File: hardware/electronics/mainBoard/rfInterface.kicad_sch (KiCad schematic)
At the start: 21 parts, among them J15 CONMHF1-SMD-T, J16 CONMHF1-SMD-T, J17 CONMHF1-SMD-T, J18 CONMHF1-SMD-T, U17 PMA2-162LNA+, U18 QCN-19D+

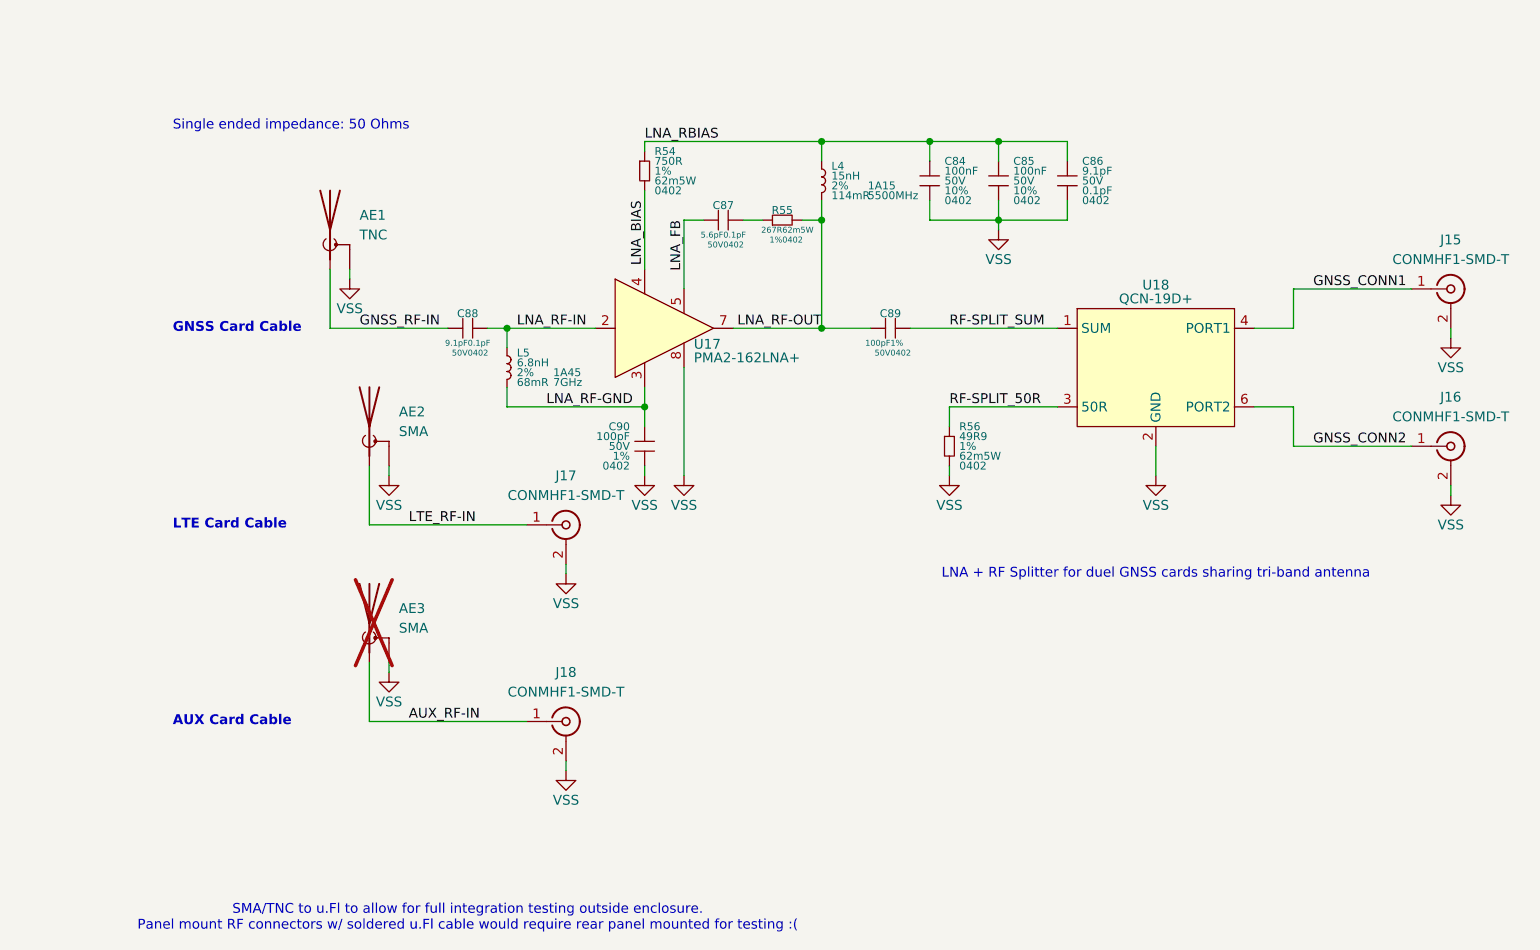
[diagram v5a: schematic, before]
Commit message: renumber references
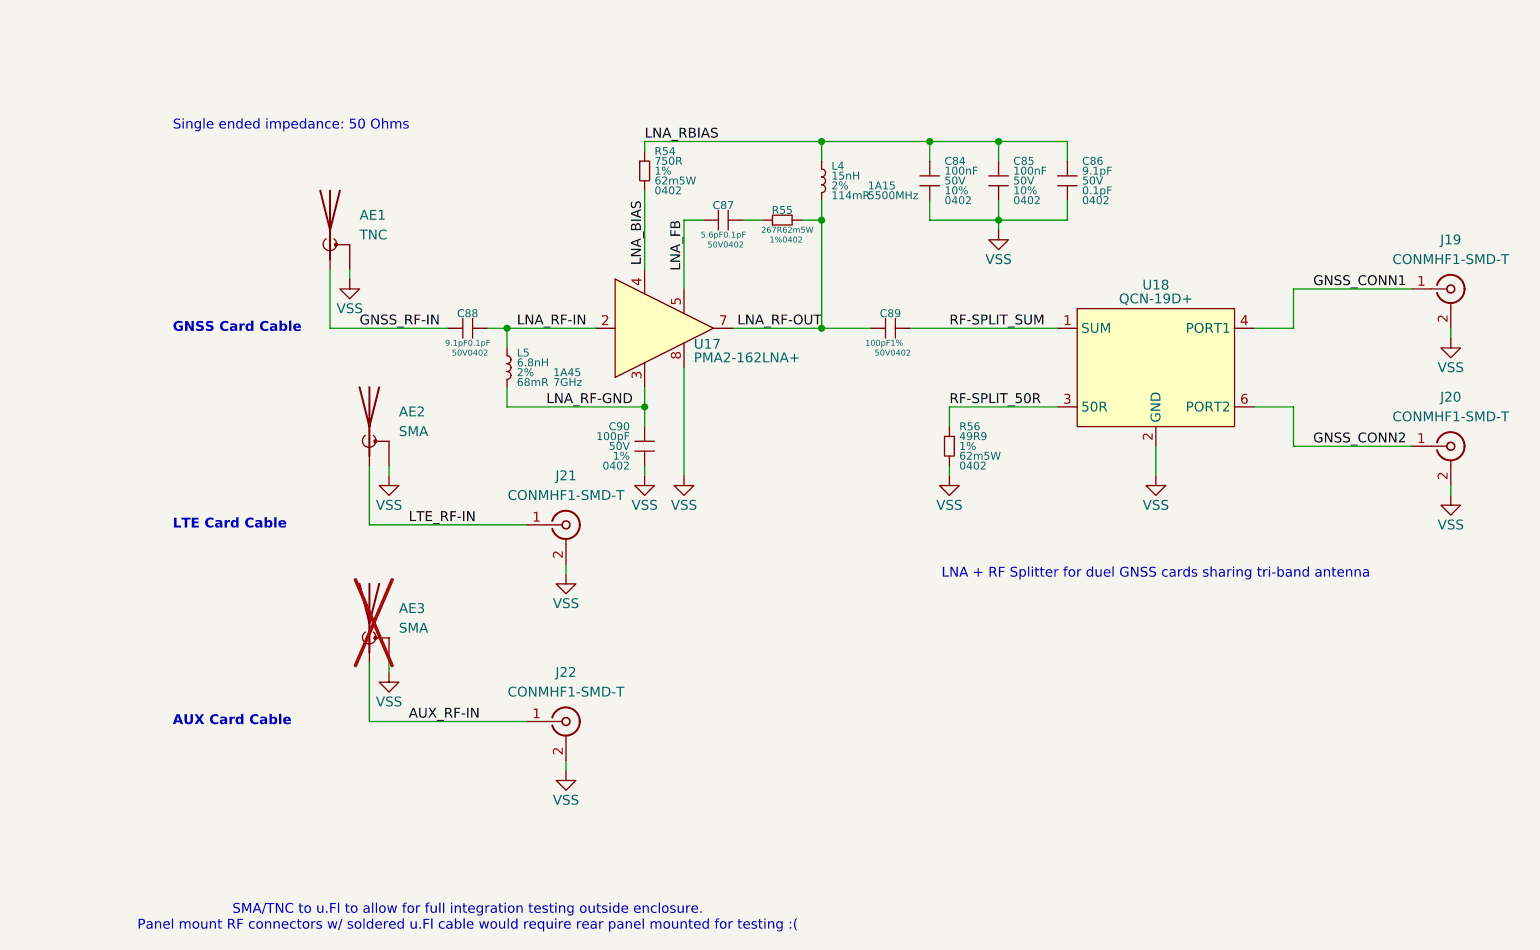
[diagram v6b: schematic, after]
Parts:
- renumbered J15 to J19, J16 to J20, J17 to J21, J18 to J22
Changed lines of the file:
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@@
 		(dnp no)
 		(fields_autoplaced yes)
-		(property "Reference" "#PWR0208"
+		(property "Reference" "#PWR0216"
 			(at 114.3 133.35 0)
 			(effects
@@
 			(project "mainBoard"
 				(path "/be16e32f-2ccf-4272-9ec7-94d5fe7a55e0/9566ea48-a930-4cf1-864c-3e42d00ab717"
-					(reference "#PWR0208")
+					(reference "#PWR0216")
 					(unit 1)
 				)
@@
 		(dnp no)
 		(fields_autoplaced yes)
-		(property "Reference" "#PWR0205"
+		(property "Reference" "#PWR0213"
 			(at 228.6 97.79 0)
 			(effects
@@
 			(project "mainBoard"
 				(path "/be16e32f-2ccf-4272-9ec7-94d5fe7a55e0/9566ea48-a930-4cf1-864c-3e42d00ab717"
-					(reference "#PWR0205")
+					(reference "#PWR0213")
 					(unit 1)
 				)
@@
 		(dnp no)
 		(fields_autoplaced yes)
-		(property "Reference" "#PWR0206"
+		(property "Reference" "#PWR0214"
 			(at 114.3 107.95 0)
 			(effects
@@
 			(project "mainBoard"
 				(path "/be16e32f-2ccf-4272-9ec7-94d5fe7a55e0/9566ea48-a930-4cf1-864c-3e42d00ab717"
-					(reference "#PWR0206")
+					(reference "#PWR0214")
 					(unit 1)
 				)
@@
 		(dnp no)
 		(fields_autoplaced yes)
-		(property "Reference" "#PWR0207"
+		(property "Reference" "#PWR0215"
 			(at 91.44 120.65 0)
 			(effects
@@
 			(project "mainBoard"
 				(path "/be16e32f-2ccf-4272-9ec7-94d5fe7a55e0/9566ea48-a930-4cf1-864c-3e42d00ab717"
-					(reference "#PWR0207")
+					(reference "#PWR0215")
 					(unit 1)
 				)
@@
 		(on_board yes)
 		(dnp no)
-		(property "Reference" "J18"
+		(property "Reference" "J22"
 			(at 114.3 120.65 0)
 			(effects
@@
 			(project "mainBoard"
 				(path "/be16e32f-2ccf-4272-9ec7-94d5fe7a55e0/9566ea48-a930-4cf1-864c-3e42d00ab717"
-					(reference "J18")
+					(reference "J22")
 					(unit 1)
 				)
@@
 		(on_board yes)
 		(dnp no)
-		(property "Reference" "J15"
+		(property "Reference" "J19"
 			(at 228.6 64.77 0)
 			(effects
@@
 			(project ""
 				(path "/be16e32f-2ccf-4272-9ec7-94d5fe7a55e0/9566ea48-a930-4cf1-864c-3e42d00ab717"
-					(reference "J15")
+					(reference "J19")
 					(unit 1)
 				)
@@
 		(dnp no)
 		(fields_autoplaced yes)
-		(property "Reference" "#PWR0200"
+		(property "Reference" "#PWR0208"
 			(at 91.44 95.25 0)
 			(effects
@@
 			(project "mainBoard"
 				(path "/be16e32f-2ccf-4272-9ec7-94d5fe7a55e0/9566ea48-a930-4cf1-864c-3e42d00ab717"
-					(reference "#PWR0200")
+					(reference "#PWR0208")
 					(unit 1)
 				)
@@
 		(dnp no)
 		(fields_autoplaced yes)
-		(property "Reference" "#PWR0198"
+		(property "Reference" "#PWR0206"
 			(at 86.36 69.85 0)
 			(effects
@@
 			(project "mainBoard"
 				(path "/be16e32f-2ccf-4272-9ec7-94d5fe7a55e0/9566ea48-a930-4cf1-864c-3e42d00ab717"
-					(reference "#PWR0198")
+					(reference "#PWR0206")
 					(unit 1)
 				)
@@
 		(on_board yes)
 		(dnp no)
-		(property "Reference" "J16"
+		(property "Reference" "J20"
 			(at 228.6 85.09 0)
 			(effects
@@
 			(project "mainBoard"
 				(path "/be16e32f-2ccf-4272-9ec7-94d5fe7a55e0/9566ea48-a930-4cf1-864c-3e42d00ab717"
-					(reference "J16")
+					(reference "J20")
 					(unit 1)
 				)
@@
 		(dnp no)
 		(fields_autoplaced yes)
-		(property "Reference" "#PWR0203"
+		(property "Reference" "#PWR0211"
 			(at 163.83 95.25 0)
 			(effects
@@
 			(project "mainBoard"
 				(path "/be16e32f-2ccf-4272-9ec7-94d5fe7a55e0/9566ea48-a930-4cf1-864c-3e42d00ab717"
-					(reference "#PWR0203")
+					(reference "#PWR0211")
 					(unit 1)
 				)
@@
 		(dnp no)
 		(fields_autoplaced yes)
-		(property "Reference" "#PWR0199"
+		(property "Reference" "#PWR0207"
 			(at 228.6 77.47 0)
 			(effects
@@
 			(project "mainBoard"
 				(path "/be16e32f-2ccf-4272-9ec7-94d5fe7a55e0/9566ea48-a930-4cf1-864c-3e42d00ab717"
-					(reference "#PWR0199")
+					(reference "#PWR0207")
 					(unit 1)
 				)
@@
 		(dnp no)
 		(fields_autoplaced yes)
-		(property "Reference" "#PWR0197"
+		(property "Reference" "#PWR0205"
 			(at 170.18 63.5 0)
 			(effects
@@
 			(project "mainBoard"
 				(path "/be16e32f-2ccf-4272-9ec7-94d5fe7a55e0/9566ea48-a930-4cf1-864c-3e42d00ab717"
-					(reference "#PWR0197")
+					(reference "#PWR0205")
 					(unit 1)
 				)
@@
 		(dnp no)
 		(fields_autoplaced yes)
-		(property "Reference" "#PWR0201"
+		(property "Reference" "#PWR0209"
 			(at 124.46 95.25 0)
 			(effects
@@
 			(project "mainBoard"
 				(path "/be16e32f-2ccf-4272-9ec7-94d5fe7a55e0/9566ea48-a930-4cf1-864c-3e42d00ab717"
-					(reference "#PWR0201")
+					(reference "#PWR0209")
 					(unit 1)
 				)
@@
 		(dnp no)
 		(fields_autoplaced yes)
-		(property "Reference" "#PWR0204"
+		(property "Reference" "#PWR0212"
 			(at 190.5 95.25 0)
 			(effects
@@
 			(project "mainBoard"
 				(path "/be16e32f-2ccf-4272-9ec7-94d5fe7a55e0/9566ea48-a930-4cf1-864c-3e42d00ab717"
-					(reference "#PWR0204")
+					(reference "#PWR0212")
 					(unit 1)
 				)
@@
 		(on_board yes)
 		(dnp no)
-		(property "Reference" "J17"
+		(property "Reference" "J21"
 			(at 114.3 95.25 0)
 			(effects
@@
 			(project "mainBoard"
 				(path "/be16e32f-2ccf-4272-9ec7-94d5fe7a55e0/9566ea48-a930-4cf1-864c-3e42d00ab717"
-					(reference "J17")
+					(reference "J21")
 					(unit 1)
 				)
@@
 		(dnp no)
 		(fields_autoplaced yes)
-		(property "Reference" "#PWR0202"
+		(property "Reference" "#PWR0210"
 			(at 129.54 95.25 0)
 			(effects
@@
 			(project "mainBoard"
 				(path "/be16e32f-2ccf-4272-9ec7-94d5fe7a55e0/9566ea48-a930-4cf1-864c-3e42d00ab717"
-					(reference "#PWR0202")
-					(unit 1)
-				)
+					(reference "#PWR0210")
+					(unit 1)
+				)
